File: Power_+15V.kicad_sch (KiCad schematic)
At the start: 58 parts, among them Q1 STB35NF10, Q2 BC858, Q3 SUD50N04, U10 LMV321RILT, U11 LM25118, U12 TL431

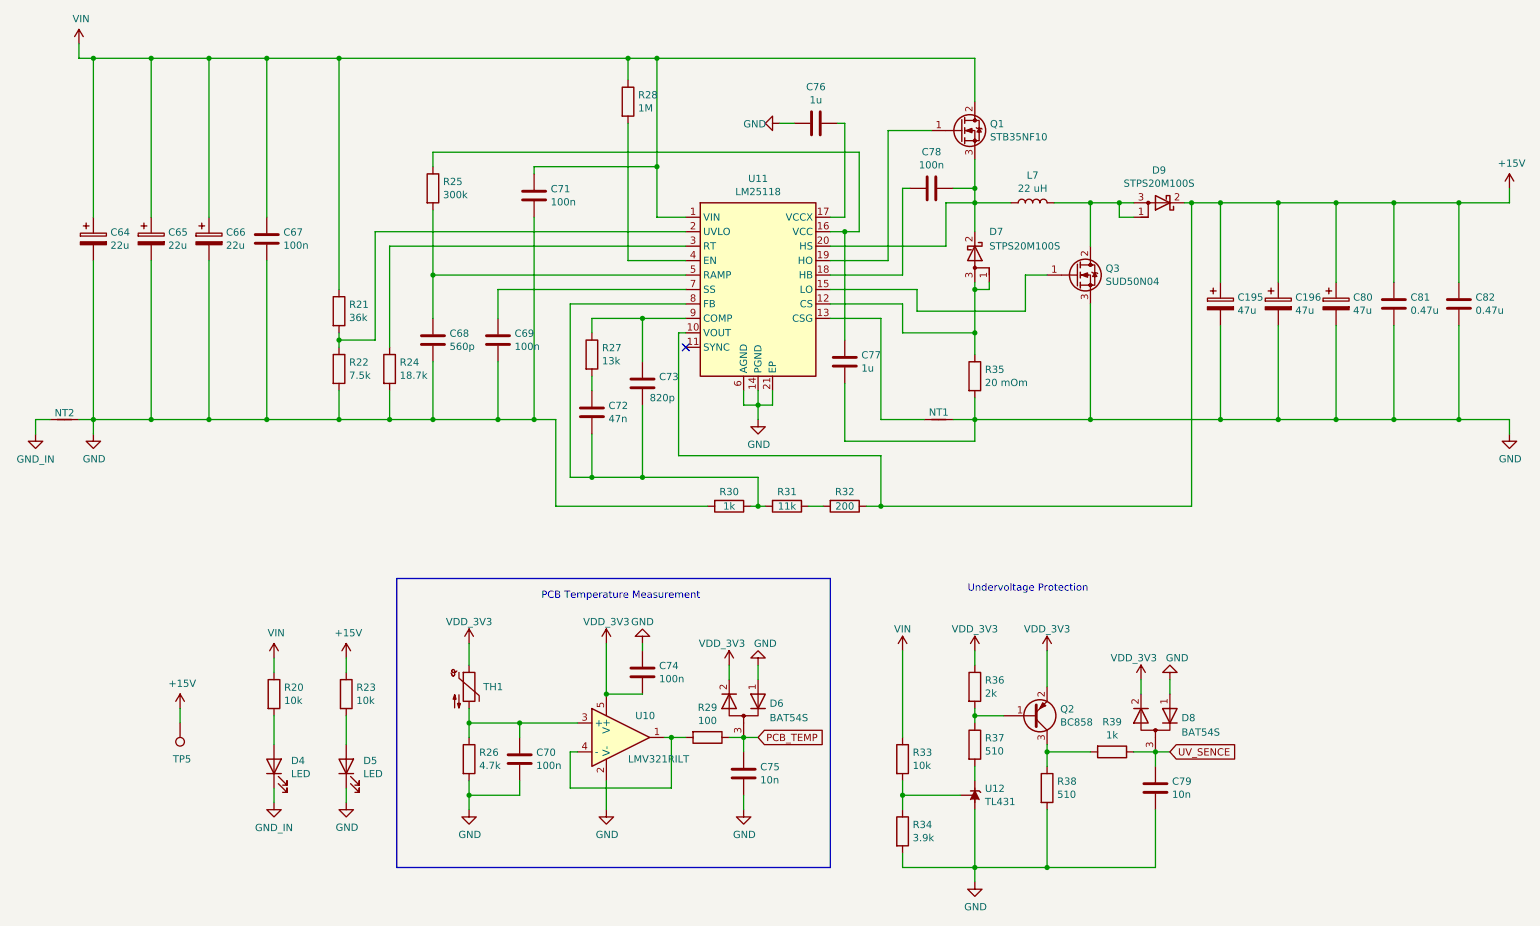
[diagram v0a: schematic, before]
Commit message: Изменения в схеме: убрал разъемы датчиков тока
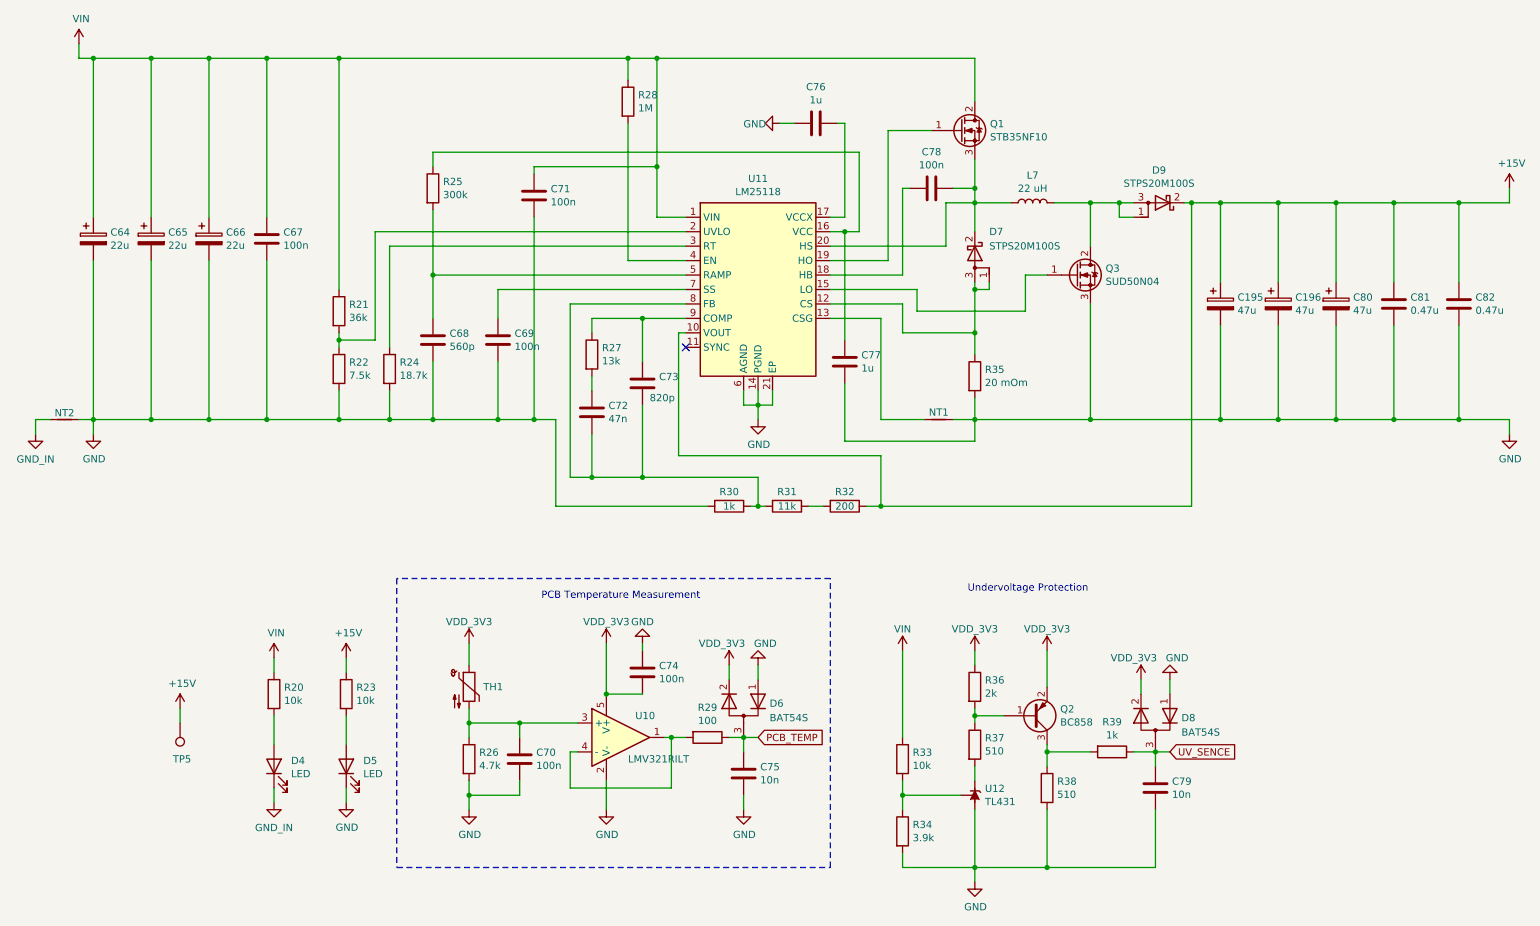
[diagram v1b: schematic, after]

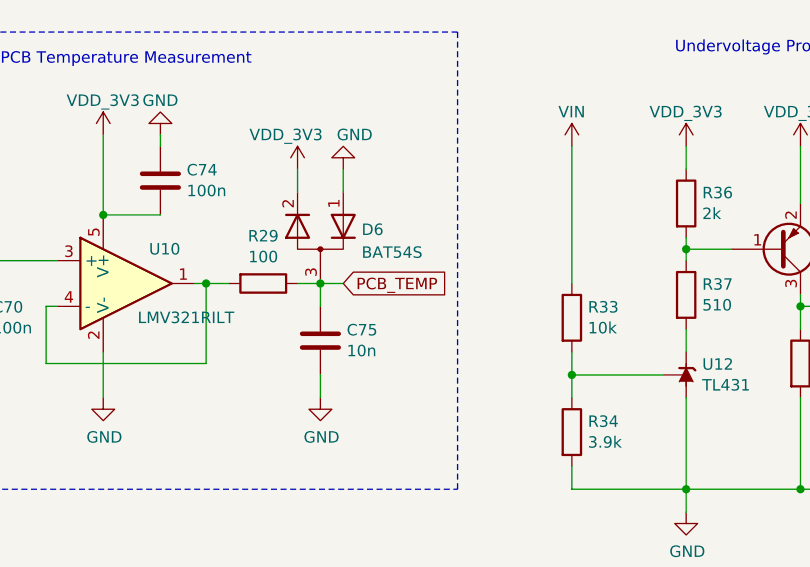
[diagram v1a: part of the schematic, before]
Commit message: Исправление: в схеме добавил обработку температур, изменил обработку токов
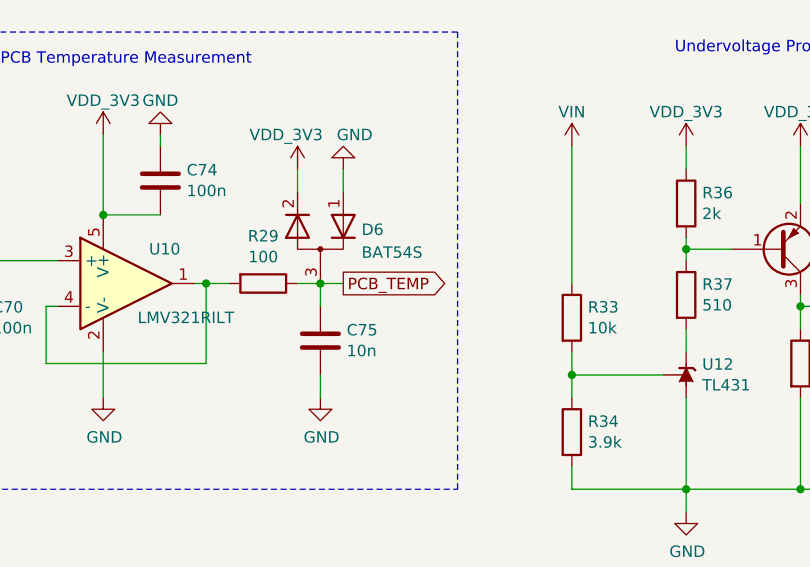
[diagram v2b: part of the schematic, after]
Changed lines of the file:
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@@
 	)
 	(global_label "PCB_TEMP"
-		(shape input)
+		(shape output)
 		(at 152.4 154.94 0)
 		(fields_autoplaced yes)
@@
 		)
 		(property "Intersheetrefs" "${INTERSHEET_REFS}"
-			(at 50.8 -12.7 0)
+			(at 165.0008 154.94 0)
 			(effects
 				(font
 					(size 1.27 1.27)
 				)
+				(justify left)
 				(hide yes)
 			)

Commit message: Изменения: развел все
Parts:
- R20: value 10k -> 4.7k
- R23: value 10k -> 3k
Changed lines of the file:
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@@
 			)
 		)
-		(property "Value" "10k"
+		(property "Value" "4.7k"
 			(at 69.088 148.463 0)
 			(effects
@@
 			)
 		)
-		(property "Value" "10k"
+		(property "Value" "3k"
 			(at 81.788 148.463 0)
 			(effects

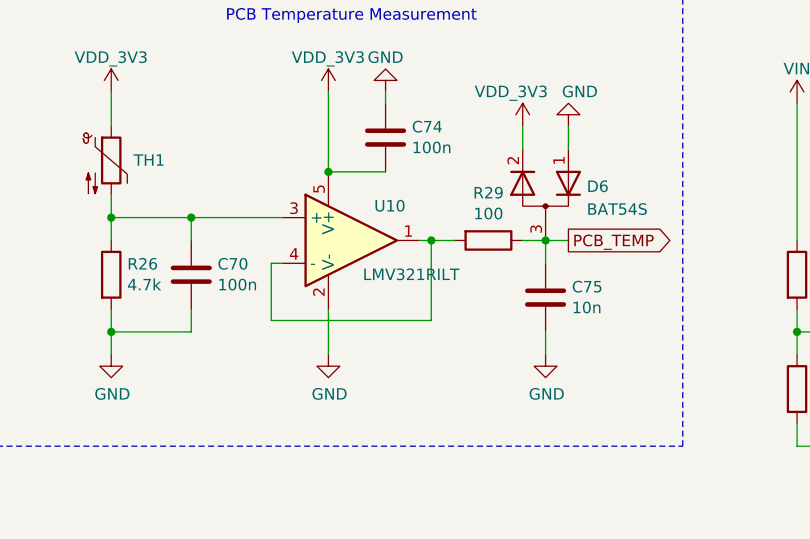
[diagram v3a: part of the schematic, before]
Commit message: Изменения: добавл BOM, оформляю заказ
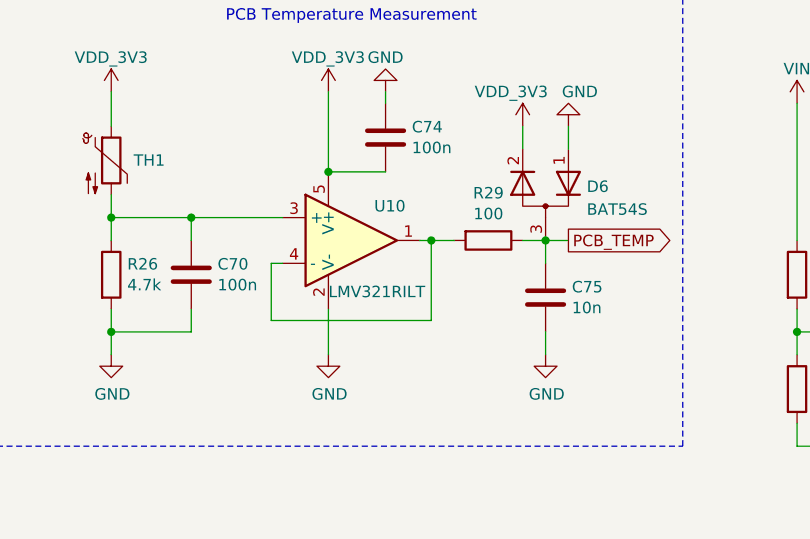
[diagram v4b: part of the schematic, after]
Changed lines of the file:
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@@
 		)
 		(property "Value" "LMV321RILT"
-			(at 129.54 158.75 0)
+			(at 125.73 160.655 0)
 			(effects
 				(font
